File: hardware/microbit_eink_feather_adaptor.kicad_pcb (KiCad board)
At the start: 2 copper layers, 78.7 x 56.5 mm, 7 parts, among them J1 feather long, J2 feather short, J3 microbit_edge_connector

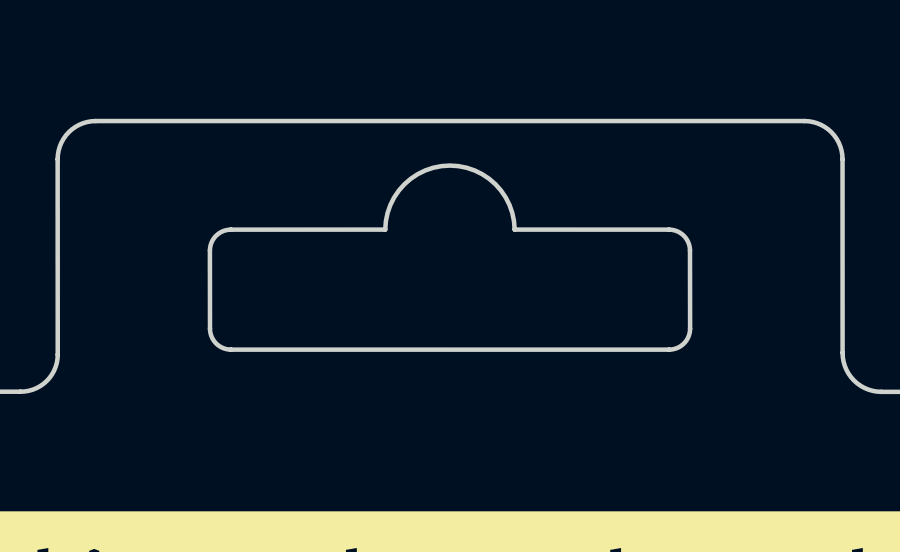
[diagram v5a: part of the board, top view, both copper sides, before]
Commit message: pcb: Replace butterfly hole with custom footprint.
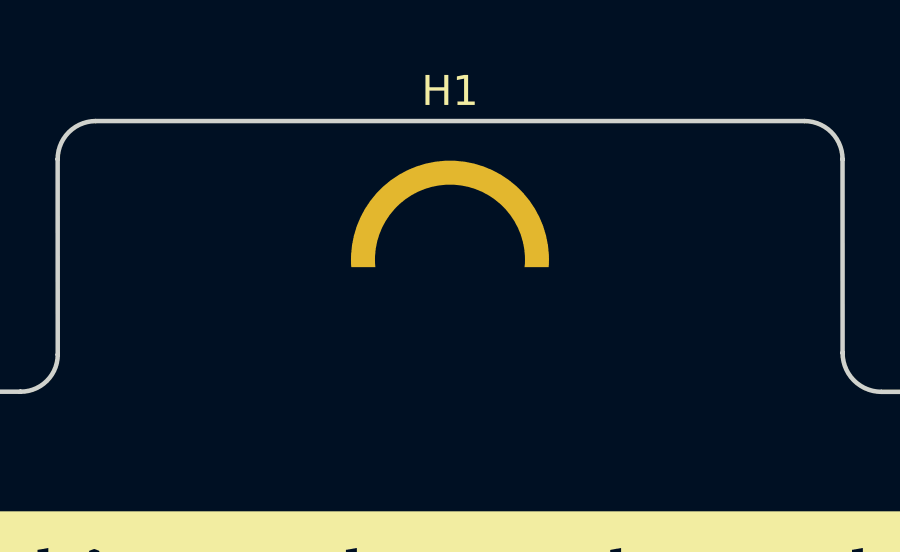
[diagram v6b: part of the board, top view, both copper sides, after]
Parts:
- added H1: Butterfly Hole, project_library:butterfly_hole, F.Cu at (90.8, 49.8)
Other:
- outline, holes or cut-outs redrawn
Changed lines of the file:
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@@
     (attr board_only exclude_from_pos_files exclude_from_bom)
     (fp_text reference "kibuzzard-62B8B88C" (at 0 -5.533086) (layer "F.SilkS") hide
-      (effects (font (size 0 0)))
+      (effects (font (size 0 0) (thickness 0.15)))
     )
     (fp_text value "G***" (at 0 5.533086) (layer "F.SilkS") hide
-      (effects (font (size 0 0)))
+      (effects (font (size 0 0) (thickness 0.15)))
     )
     (fp_poly (pts
@@
       ) (layer "F.SilkS") (width 0) (fill solid))
   )
+  (footprint "project_library:butterfly_hole" (layer "F.Cu")
+    (at 90.8 49.8)
+    (property "Sheetfile" "microbit_eink_feather_adaptor.kicad_sch")
+    (property "Sheetname" "")
+    (attr through_hole)
+    (fp_text reference "H1" (at 0 -7.62 unlocked) (layer "F.SilkS")
+      (effects (font (size 1 1) (thickness 0.15)))
+    )
+    (fp_text value "Butterfly Hole" (at 0 7.62 unlocked) (layer "F.Fab")
+      (effects (font (size 1 1) (thickness 0.15)))
+    )
+    (fp_text user "${REFERENCE}" (at 0 5.08 unlocked) (layer "F.Fab")
+      (effects (font (size 1 1) (thickness 0.15)))
+    )
+    (pad "" np_thru_hole oval (at 0 0) (size 17.6 5.1) (drill oval 16 3.5) (layers F&B.Cu *.Mask))
+    (pad "" np_thru_hole circle (at 0 -2) (size 6.6 6.6) (drill 5) (layers F&B.Cu *.Mask))
+  )
   (footprint "Connector_PinHeader_2.54mm:PinHeader_1x16_P2.54mm_Vertical" (layer "B.Cu")
     (at 95.25 97.79 90)
@@
   (gr_arc (start 130.175 97.263949) (mid 129.424162 99.021903) (end 127.635 99.695) (layer "Edge.Cuts") (width 0.15))
   (gr_arc (start 102.615011 43.18) (mid 103.513037 43.551974) (end 103.885011 44.45) (layer "Edge.Cuts") (width 0.15))
-  (gr_arc (start 88.64192 46.79848) (mid 90.798745 44.663839) (end 92.955607 46.79848) (layer "Edge.Cuts") (width 0.15))
   (gr_arc (start 51.435 66.675) (mid 52.178949 64.878949) (end 53.975 64.135) (layer "Edge.Cuts") (width 0.15))
   (gr_arc (start 77.725546 50.965798) (mid 77.360043 51.843255) (end 76.479702 52.201759) (layer "Edge.Cuts") (width 0.15))
   (gr_line (start 130.175 66.675) (end 130.175 97.263949) (layer "Edge.Cuts") (width 0.2))
-  (gr_arc (start 98.80384 50.09986) (mid 98.598815 50.594835) (end 98.10384 50.79986) (layer "Edge.Cuts") (width 0.15))
-  (gr_line (start 88.64192 46.79848) (end 83.497573 46.799707) (layer "Edge.Cuts") (width 0.15))
   (gr_line (start 62.3 54.61) (end 62.303384 61.704922) (layer "Edge.Cuts") (width 0.15))
   (gr_line (start 103.885011 44.45) (end 103.886989 50.906871) (layer "Edge.Cuts") (width 0.15))
-  (gr_arc (start 98.100636 46.799131) (mid 98.595611 47.004156) (end 98.800636 47.499131) (layer "Edge.Cuts") (width 0.15))
-  (gr_line (start 82.800505 50.099494) (end 82.797573 47.499707) (layer "Edge.Cuts") (width 0.15))
-  (gr_line (start 98.100636 46.799131) (end 92.955607 46.79848) (layer "Edge.Cuts") (width 0.15))
   (gr_arc (start 116.8 52.2) (mid 118.580337 52.916849) (end 119.3 54.696051) (layer "Edge.Cuts") (width 0.15))
   (gr_line (start 76.479702 52.201759) (end 64.77 52.2) (layer "Edge.Cuts") (width 0.15))
@@
   (gr_arc (start 105.182405 52.206699) (mid 104.264847 51.82572) (end 103.886989 50.906871) (layer "Edge.Cuts") (width 0.15))
   (gr_line (start 127.635 64.135) (end 121.728786 64.134015) (layer "Edge.Cuts") (width 0.15))
-  (gr_arc (start 83.500505 50.799494) (mid 83.00553 50.594469) (end 82.800505 50.099494) (layer "Edge.Cuts") (width 0.15))
-  (gr_line (start 98.80384 50.09986) (end 98.800636 47.499131) (layer "Edge.Cuts") (width 0.15))
   (gr_line (start 116.8 52.2) (end 105.182405 52.206699) (layer "Edge.Cuts") (width 0.15))
   (gr_arc (start 127.635 64.135) (mid 129.431051 64.878949) (end 130.175 66.675) (layer "Edge.Cuts") (width 0.15))
@@
   (gr_arc (start 77.722454 44.45) (mid 78.094428 43.551974) (end 78.992454 43.18) (layer "Edge.Cuts") (width 0.15))
   (gr_line (start 127.635 99.695) (end 53.866051 99.695) (layer "Edge.Cuts") (width 0.2))
-  (gr_line (start 98.10384 50.79986) (end 83.500505 50.799494) (layer "Edge.Cuts") (width 0.15))
   (gr_arc (start 53.866051 99.695) (mid 52.108097 98.944162) (end 51.435 97.155) (layer "Edge.Cuts") (width 0.15))
   (gr_line (start 53.975 64.135) (end 59.763384 64.135973) (layer "Edge.Cuts") (width 0.2))
   (gr_line (start 51.435 97.155) (end 51.435 66.675) (layer "Edge.Cuts") (width 0.2))
-  (gr_arc (start 82.797573 47.499707) (mid 83.002598 47.004732) (end 83.497573 46.799707) (layer "Edge.Cuts") (width 0.15))
   (gr_arc (start 121.728786 64.134015) (mid 119.970854 63.383155) (end 119.297735 61.594015) (layer "Edge.Cuts") (width 0.15))
   (gr_text "JLCJLCJLCJLC" (at 122.555 97.536) (layer "B.SilkS")

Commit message: schematic & pcb: Add (optional) header to physically hold battery.
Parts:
- added J4: N/C (battery holder), Connector_PinHeader_2.54mm:PinHeader_1x04_P2.54mm_Vertical, B.Cu at (113.0, 97.8)
- moved kibuzzard-62B89D05 0.43 mm to (125.9, 97.8)
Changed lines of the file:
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@@
   (net 86 "unconnected-(J3-Pad79)")
   (net 87 "unconnected-(J3-Pad80)")
+  (net 88 "unconnected-(J4-Pad1)")
+  (net 89 "unconnected-(J4-Pad2)")
+  (net 90 "unconnected-(J4-Pad3)")
+  (net 91 "unconnected-(J4-Pad4)")
   (footprint "MountingHole:MountingHole_2.7mm_M2.5" locked (layer "F.Cu")
     (at 53.975 66.675)
@@
   )
   (footprint "kibuzzard-62B89D05" (layer "F.Cu")
-    (at 126.238 97.536)
+    (at 125.9 97.8)
     (descr "Generated with KiBuzzard")
     (tags "kb_params=eyJBbGlnbm1lbnRDaG9pY2UiOiAiQ2VudGVyIiwgIkNhcExlZnRDaG9pY2UiOiAiKCIsICJDYXBSaWdodENob2ljZSI6ICIpIiwgIkZvbnRDb21ib0JveCI6ICJGcmVkb2thT25lIiwgIkhlaWdodEN0cmwiOiAiMSIsICJMYXllckNvbWJvQm94IjogIkYuU2lsa1MiLCAiTXVsdGlMaW5lVGV4dCI6ICJ2MS4xIiwgIlBhZGRpbmdCb3R0b21DdHJsIjogIjUiLCAiUGFkZGluZ0xlZnRDdHJsIjogIjUiLCAiUGFkZGluZ1JpZ2h0Q3RybCI6ICI1IiwgIlBhZGRpbmdUb3BDdHJsIjogIjUiLCAiV2lkdGhDdHJsIjogIjEifQ==")
@@
       (net 28 "/VBAT") (pinfunction "Pin_12") (pintype "passive"))
     (model "${KICAD6_3DMODEL_DIR}/Connector_PinHeader_2.54mm.3dshapes/PinHeader_1x12_P2.54mm_Vertical.wrl"
+      (offset (xyz 0 0 0))
+      (scale (xyz 1 1 1))
+      (rotate (xyz 0 0 0))
+    )
+  )
+  (footprint "Connector_PinHeader_2.54mm:PinHeader_1x04_P2.54mm_Vertical" (layer "B.Cu")
+    (at 113 97.8 -90)
+    (descr "Through hole straight pin header, 1x04, 2.54mm pitch, single row")
+    (tags "Through hole pin header THT 1x04 2.54mm single row")
+    (property "Sheetfile" "microbit_eink_feather_adaptor.kicad_sch")
+    (property "Sheetname" "")
+    (attr through_hole)
+    (fp_text reference "J4" (at 0 -10.4 180) (layer "B.SilkS")
+      (effects (font (size 1 1) (thickness 0.15)) (justify mirror))
+    )
+    (fp_text value "N/C (battery holder)" (at 0 -9.95 90) (layer "B.Fab")
+      (effects (font (size 1 1) (thickness 0.15)) (justify mirror))
+    )
+    (fp_text user "${REFERENCE}" (at 0 -3.81 180) (layer "B.Fab")
+      (effects (font (size 1 1) (thickness 0.15)) (justify mirror))
+    )
+    (fp_line (start -1.33 -1.27) (end 1.33 -1.27) (layer "B.SilkS") (width 0.12))
+    (fp_line (start -1.33 1.33) (end 0 1.33) (layer "B.SilkS") (width 0.12))
+    (fp_line (start 1.33 -1.27) (end 1.33 -8.95) (layer "B.SilkS") (width 0.12))
+    (fp_line (start -1.33 -1.27) (end -1.33 -8.95) (layer "B.SilkS") (width 0.12))
+    (fp_line (start -1.33 0) (end -1.33 1.33) (layer "B.SilkS") (width 0.12))
+    (fp_line (start -1.33 -8.95) (end 1.33 -8.95) (layer "B.SilkS") (width 0.12))
+    (fp_line (start 1.8 1.8) (end -1.8 1.8) (layer "B.CrtYd") (width 0.05))
+    (fp_line (start -1.8 -9.4) (end 1.8 -9.4) (layer "B.CrtYd") (width 0.05))
+    (fp_line (start -1.8 1.8) (end -1.8 -9.4) (layer "B.CrtYd") (width 0.05))
+    (fp_line (start 1.8 -9.4) (end 1.8 1.8) (layer "B.CrtYd") (width 0.05))
+    (fp_line (start 1.27 -8.89) (end -1.27 -8.89) (layer "B.Fab") (width 0.1))
+    (fp_line (start -0.635 1.27) (end 1.27 1.27) (layer "B.Fab") (width 0.1))
+    (fp_line (start -1.27 -8.89) (end -1.27 0.635) (layer "B.Fab") (width 0.1))
+    (fp_line (start -1.27 0.635) (end -0.635 1.27) (layer "B.Fab") (width 0.1))
+    (fp_line (start 1.27 1.27) (end 1.27 -8.89) (layer "B.Fab") (width 0.1))
+    (pad "1" thru_hole rect (at 0 0 270) (size 1.7 1.7) (drill 1) (layers *.Cu *.Mask)
+      (net 88 "unconnected-(J4-Pad1)") (pinfunction "Pin_1") (pintype "passive"))
+    (pad "2" thru_hole oval (at 0 -2.54 270) (size 1.7 1.7) (drill 1) (layers *.Cu *.Mask)
+      (net 89 "unconnected-(J4-Pad2)") (pinfunction "Pin_2") (pintype "passive"))
+    (pad "3" thru_hole oval (at 0 -5.08 270) (size 1.7 1.7) (drill 1) (layers *.Cu *.Mask)
+      (net 90 "unconnected-(J4-Pad3)") (pinfunction "Pin_3") (pintype "passive"))
+    (pad "4" thru_hole oval (at 0 -7.62 270) (size 1.7 1.7) (drill 1) (layers *.Cu *.Mask)
+      (net 91 "unconnected-(J4-Pad4)") (pinfunction "Pin_4") (pintype "passive"))
+    (model "${KICAD6_3DMODEL_DIR}/Connector_PinHeader_2.54mm.3dshapes/PinHeader_1x04_P2.54mm_Vertical.wrl"
       (offset (xyz 0 0 0))
       (scale (xyz 1 1 1))
@@
   (gr_line (start 51.435 97.155) (end 51.435 66.675) (layer "Edge.Cuts") (width 0.2))
   (gr_arc (start 121.728786 64.134015) (mid 119.970854 63.383155) (end 119.297735 61.594015) (layer "Edge.Cuts") (width 0.15))
-  (gr_text "JLCJLCJLCJLC" (at 122.555 97.536) (layer "B.SilkS")
+  (gr_text "JLCJLCJLCJLC" (at 104.1 97.8) (layer "B.SilkS")
     (effects (font (size 1 1) (thickness 0.2)) (justify mirror))
   )
